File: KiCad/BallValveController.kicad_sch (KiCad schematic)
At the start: 61 parts, among them J1 Screw_Terminal_01x03, J2 Screw_Terminal_01x04, J3 Screw_Terminal_01x04, J4 Screw_Terminal_01x04, J5 Conn_01x01_Male, J6 Screw_Terminal_01x04, J7 Screw_Terminal_01x02, K1 G5V-2, Q1 Q_PMOS_GDS, Q2 2N2222A, U1 MT2499A, U2 L7805, U3 XIAO-ESP32-C6

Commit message: DRC with TPC561201/08
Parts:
- removed C3: 22nF, Capacitor_SMD:C_0805_2012Metric_Pad1.18x1.45mm_HandSolder, symbol Device:C_Small
- removed U1: MT2499A, Package_SO:TI_SO-PowerPAD-8, symbol custom_kicad_lib_sk:MT499A
- added U4: TPS561201 or 08, Package_TO_SOT_SMD:SOT-23-6, symbol Regulator_Switching:TPS562200
- L1: value 10uH -> 4.7uH
- L2: value 22uH -> 10uH
- R4: value 15k -> 12k
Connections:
- net GND: now also U4.1 (GND)
- net IND1: now also U4.2 (SW)
- net PwrIn: now also U4.3 (VIN), U4.5 (EN)
- net at R3.2, R4.1: now also U4.4 (VFB)
- net at C2.1: now also U4.6 (VBST)
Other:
- moved on the sheet: C2

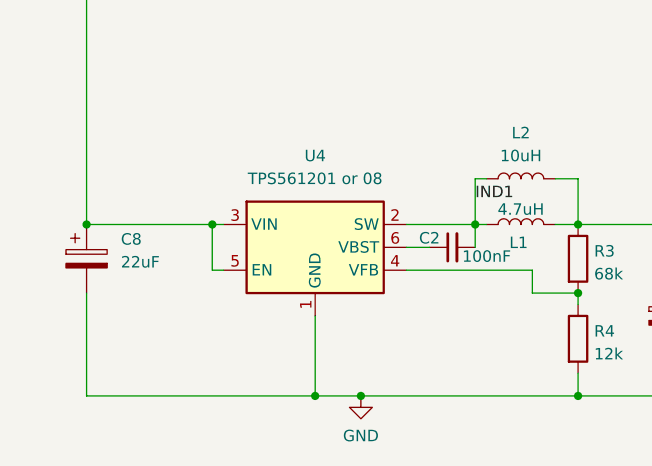
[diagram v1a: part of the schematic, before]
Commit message: Added EN resistor for buck converter
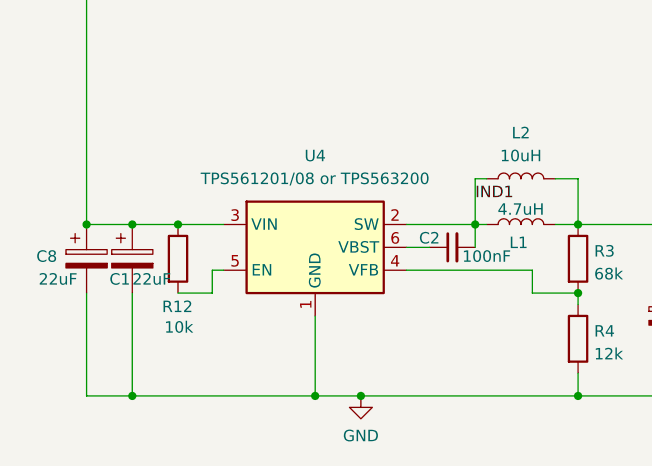
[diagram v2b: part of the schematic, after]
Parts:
- added C1: 22uF, Capacitor_SMD:C_1206_3216Metric_Pad1.33x1.80mm_HandSolder, symbol Device:C_Polarized
- added R12: 10k, Resistor_SMD:R_0805_2012Metric_Pad1.20x1.40mm_HandSolder, symbol Device:R
- U4: value TPS561201 or 08 -> TPS561201/08 or TPS563200
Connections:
- net GND: now also C1.2
- net PwrIn: now also C1.1, R12.1; no longer U4.5 (EN)
- new net: R12.2, U4.5 (EN)
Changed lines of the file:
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@@
 	)
 	(junction
-		(at 35.56 170.18)
+		(at 167.64 133.35)
 		(diameter 0)
 		(color 0 0 0 0)
 	)
 	(junction
-		(at 167.64 133.35)
+		(at 220.98 134.62)
 		(diameter 0)
 		(color 0 0 0 0)
 	)
 	(junction
-		(at 220.98 134.62)
+		(at 264.16 124.46)
 		(diameter 0)
 		(color 0 0 0 0)
 	)
 	(junction
-		(at 264.16 124.46)
+		(at 31.75 170.18)
+		(diameter 0)
+		(color 0 0 0 0)
+	)
+	(junction
+		(at 26.67 170.18)
 		(diameter 0)
 		(color 0 0 0 0)
@@
 	)
 	(junction
+		(at 26.67 189.23)
+		(diameter 0)
+		(color 0 0 0 0)
+	)
+	(junction
 		(at 76.2 177.8)
 		(diameter 0)
@@
 	(wire
 		(pts
+			(xy 26.67 170.18) (xy 31.75 170.18)
+		)
+		(stroke
+			(width 0)
+			(type default)
+		)
+	)
+	(wire
+		(pts
 			(xy 139.7 41.91) (xy 139.7 46.99)
 		)
@@
 	(wire
 		(pts
+			(xy 35.56 175.26) (xy 35.56 177.8)
+		)
+		(stroke
+			(width 0)
+			(type default)
+		)
+	)
+	(wire
+		(pts
 			(xy 77.47 55.88) (xy 77.47 60.96)
 		)
@@
 	(wire
 		(pts
+			(xy 26.67 189.23) (xy 21.59 189.23)
+		)
+		(stroke
+			(width 0)
+			(type default)
+		)
+	)
+	(wire
+		(pts
 			(xy 64.77 172.72) (xy 64.77 170.18)
 		)
@@
 	(wire
 		(pts
-			(xy 35.56 170.18) (xy 36.83 170.18)
+			(xy 31.75 170.18) (xy 36.83 170.18)
 		)
 		(stroke
@@
 	(wire
 		(pts
-			(xy 35.56 170.18) (xy 35.56 175.26)
-		)
-		(stroke
-			(width 0)
-			(type default)
-		)
-	)
-	(wire
-		(pts
 			(xy 102.87 93.98) (xy 132.08 93.98)
 		)
@@
 	(wire
 		(pts
+			(xy 31.75 177.8) (xy 35.56 177.8)
+		)
+		(stroke
+			(width 0)
+			(type default)
+		)
+	)
+	(wire
+		(pts
 			(xy 137.16 99.06) (xy 137.16 106.68)
 		)
@@
 	(wire
 		(pts
-			(xy 46.99 189.23) (xy 21.59 189.23)
+			(xy 46.99 189.23) (xy 26.67 189.23)
 		)
 		(stroke
@@
 	(wire
 		(pts
-			(xy 21.59 170.18) (xy 35.56 170.18)
+			(xy 21.59 170.18) (xy 26.67 170.18)
 		)
 		(stroke
@@
 	(wire
 		(pts
+			(xy 26.67 177.8) (xy 26.67 189.23)
+		)
+		(stroke
+			(width 0)
+			(type default)
+		)
+	)
+	(wire
+		(pts
 			(xy 46.99 180.34) (xy 46.99 189.23)
 		)
@@
 		(on_board yes)
 		(dnp no)
-		(fields_autoplaced yes)
 		(property "Reference" "C8"
-			(at 25.4 171.8309 0)
+			(at 16.002 173.736 0)
 			(effects
 				(font
@@
 		)
 		(property "Value" "22uF"
-			(at 25.4 174.3709 0)
+			(at 16.256 176.276 0)
 			(effects
 				(font
@@
 	)
 	(symbol
+		(lib_id "Device:R")
+		(at 31.75 173.99 0)
+		(unit 1)
+		(exclude_from_sim no)
+		(in_bom yes)
+		(on_board yes)
+		(dnp no)
+		(property "Reference" "R12"
+			(at 29.972 179.324 0)
+			(effects
+				(font
+					(size 1.27 1.27)
+				)
+				(justify left)
+			)
+		)
+		(property "Value" "10k"
+			(at 30.226 181.61 0)
+			(effects
+				(font
+					(size 1.27 1.27)
+				)
+				(justify left)
+			)
+		)
+		(property "Footprint" "Resistor_SMD:R_0805_2012Metric_Pad1.20x1.40mm_HandSolder"
+			(at 29.972 173.99 90)
+			(effects
+				(font
+					(size 1.27 1.27)
+				)
+				(hide yes)
+			)
+		)
+		(property "Datasheet" "~"
+			(at 31.75 173.99 0)
+			(effects
+				(font
+					(size 1.27 1.27)
+				)
+				(hide yes)
+			)
+		)
+		(property "Description" "Resistor"
+			(at 31.75 173.99 0)
+			(effects
+				(font
+					(size 1.27 1.27)
+				)
+				(hide yes)
+			)
+		)
+		(property "JLCPCB Part#" "C4328"
+			(at 31.75 173.99 0)
+			(effects
+				(font
+					(size 1.27 1.27)
+				)
+				(hide yes)
+			)
+		)
+		(pin "1"
+		)
+		(pin "2"
+		)
+		(instances
+			(project "BallValveController"
+				(path "/2a5b3e3c-2022-46db-8938-2c3b2e9edb6d"
+					(reference "R12")
+					(unit 1)
+				)
+			)
+		)
+	)
+	(symbol
 		(lib_id "Connector:Conn_01x04_Pin")
 		(at 118.11 46.99 0)
@@
 			)
 		)
-		(property "Value" "TPS561201 or 08"
+		(property "Value" "TPS561201/08 or TPS563200"
 			(at 46.99 165.1 0)
 			(effects
@@
 					(unit 1)
 				)
+			)
+		)
+	)
+	(symbol
+		(lib_id "Device:C_Polarized")
+		(at 26.67 173.99 0)
+		(unit 1)
+		(exclude_from_sim no)
+		(in_bom yes)
+		(on_board yes)
+		(dnp no)
+		(property "Reference" "C1"
+			(at 24.13 176.276 0)
+			(effects
+				(font
+					(size 1.27 1.27)
+				)
+				(justify left)
+			)
+		)
+		(property "Value" "22uF"
+			(at 26.67 176.276 0)
+			(effects
+				(font
+					(size 1.27 1.27)
+				)
+				(justify left)
+			)
+		)
+		(property "Footprint" "Capacitor_SMD:C_1206_3216Metric_Pad1.33x1.80mm_HandSolder"
+			(at 27.6352 177.8 0)
+			(effects
+				(font
+					(size 1.27 1.27)
+				)
+				(hide yes)
+			)
+		)
+		(property "Datasheet" "~"
+			(at 26.67 173.99 0)
+			(effects
+				(font
+					(size 1.27 1.27)
+				)
+				(hide yes)
+			)
+		)
+		(property "Description" "Polarized capacitor"
+			(at 26.67 173.99 0)
+			(effects
+				(font
+					(size 1.27 1.27)
+				)
+				(hide yes)
+			)
+		)
+		(pin "2"
+		)
+		(pin "1"
+		)
+		(instances
+			(project "BallValveController"
+				(path "/2a5b3e3c-2022-46db-8938-2c3b2e9edb6d"
+					(reference "C1")
+					(unit 1)
+				)

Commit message: ME3116 layout
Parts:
- added 1: (no value), Package_TO_SOT_SMD:SOT-23-6, symbol LOCAL1:ME3116AM6G_0_0
- added C3: 470nF, Capacitor_SMD:C_0805_2012Metric_Pad1.18x1.45mm_HandSolder, symbol Device:C_Small
- added D4: SS34, Diode_SMD:D_SMA, symbol Diode:SS34
- added R19: 4.7k, Resistor_SMD:R_0805_2012Metric_Pad1.20x1.40mm_HandSolder, symbol Device:R
- U4: value TPS561201/08 or TPS563200 -> TPS561201/08 or TPS562203 or TPS563203; now not fitted
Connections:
- net +5V: now also 1.6 (SW), C3.1, D4.1 (K)
- net GND: now also 1.2 (GND), D4.2 (A), R19.2
- net PwrIn: now also 1.5 (VIN)
- net at R3.2, R4.1, U4.4 (VFB): now also 1.3 (FB), C3.2
- net at R12.2, U4.5 (EN): now also 1.4 (EN), R19.1
- net at C2.1, U4.6 (VBST): now also 1.1 (BS)
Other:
- moved on the sheet: C5, C6

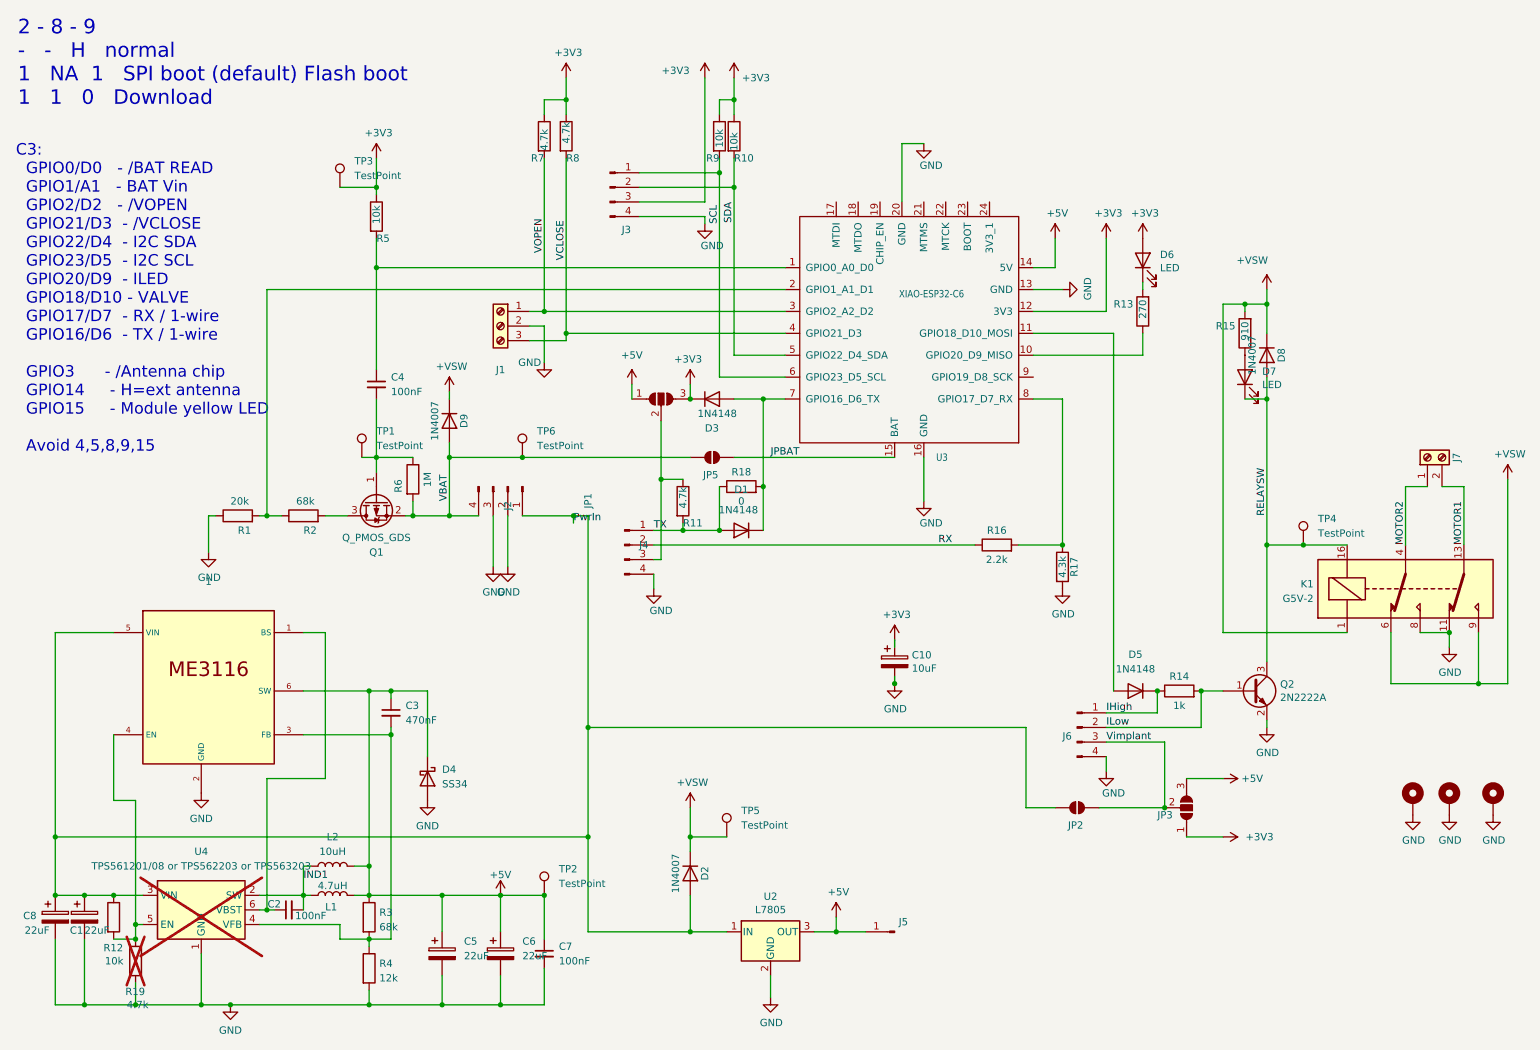
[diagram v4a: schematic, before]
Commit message: ME3116 dual layout
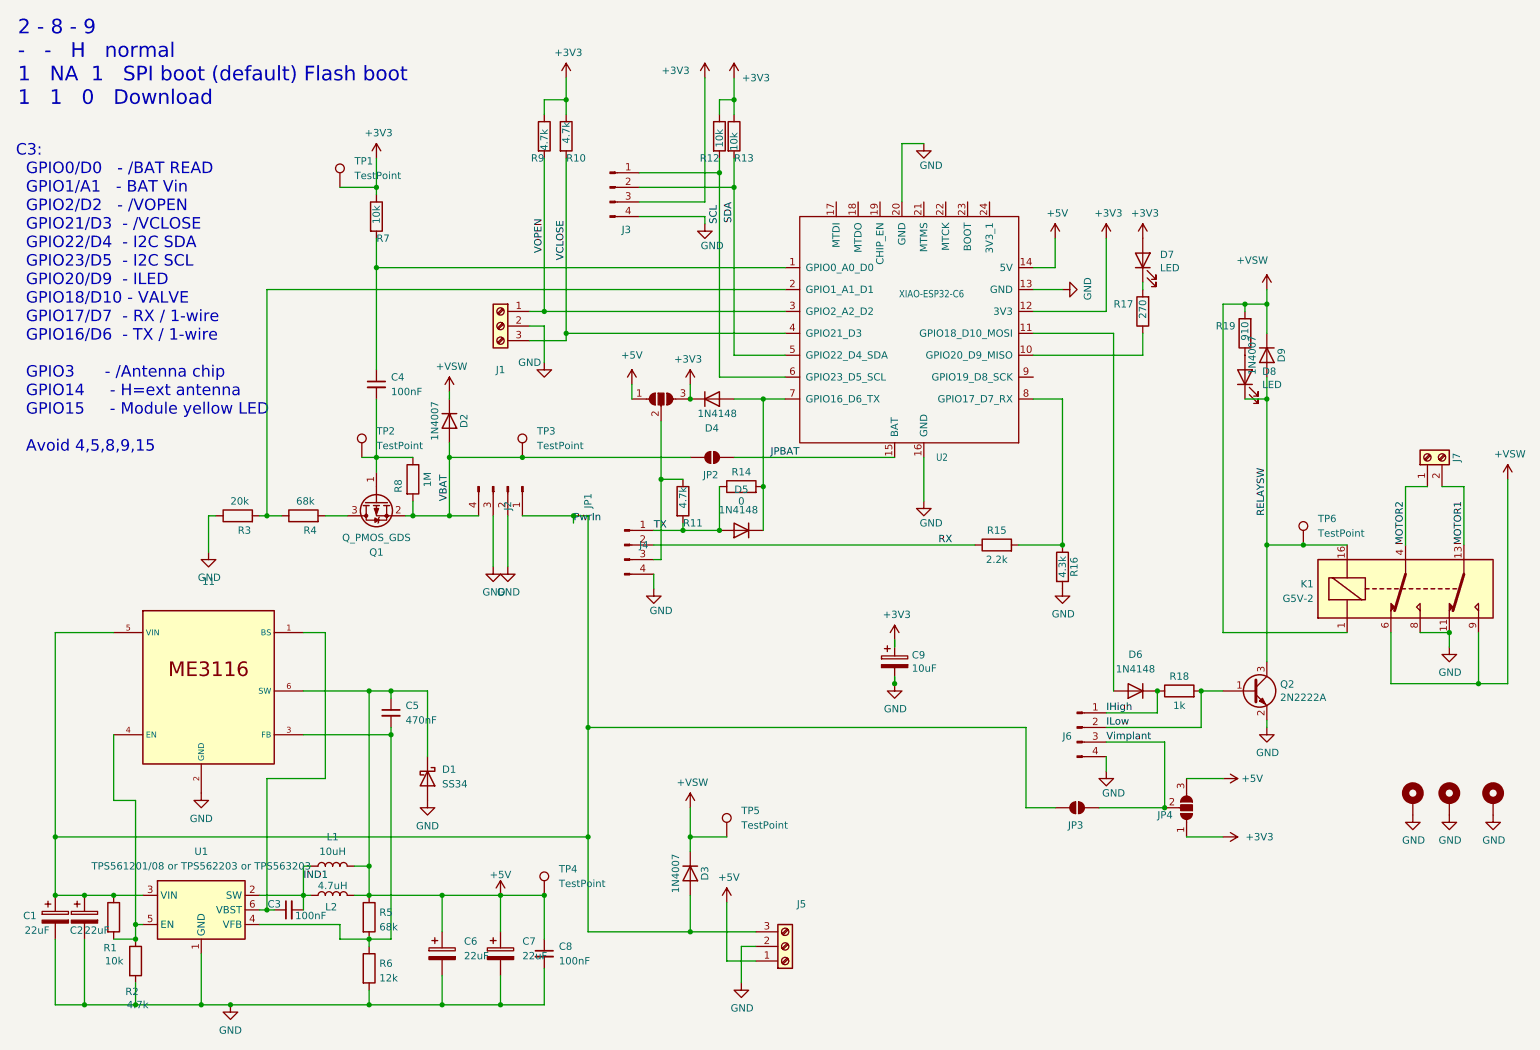
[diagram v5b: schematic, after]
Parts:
- removed J5: Conn_01x01_Male, Connector_PinHeader_2.54mm:PinHeader_1x01_P2.54mm_Vertical, symbol Connector:Conn_01x01_Male
- removed U2: L7805, Package_TO_SOT_THT:TO-220-3_Vertical, symbol Regulator_Linear:L7805
- added J5: Screw_Terminal_01x03, Connector_PinHeader_2.54mm:PinHeader_1x03_P2.54mm_Vertical, symbol Connector:Screw_Terminal_01x03
- R2: renamed from R19; now fitted
- U1: renamed from U4; now fitted
- renumbered 1 to 11, C8 to C1, C1 to C2, C2 to C3, C3 to C5, C5 to C6, C6 to C7, C7 to C8, C10 to C9, D4 to D1, D9 to D2, D2 to D3, D3 to D4, D1 to D5, D5 to D6, D6 to D7, D7 to D8, D8 to D9, H2 to H1, H1 to H2, JP5 to JP2, JP2 to JP3, JP3 to JP4, L2 to L1, L1 to L2, R12 to R1, R8 to R10, R9 to R12, R10 to R13, R18 to R14, R16 to R15, R17 to R16, R13 to R17, R14 to R18, R15 to R19, R1 to R3, R2 to R4, R3 to R5, R4 to R6, R5 to R7, R6 to R8, R7 to R9, TP3 to TP1, TP1 to TP2, TP6 to TP3, TP2 to TP4, TP4 to TP6, U3 to U2
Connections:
- net +5V: now also J5.1 (Pin_1)
- net GND: now also J5.2 (Pin_2)
- net PwrIn: now also J5.3 (Pin_3)
